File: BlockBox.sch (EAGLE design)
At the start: 95 parts, among them Q100 TK3R1E04PL, Q101 TK3R1E04PL, Q102 IPP052N06L3 G, Q103 IPP052N06L3 G, Q104 IPP052N06L3 G, Q105 IPP052N06L3 G, Q106 TK3R1E04PL, Q300 NMOS, U100 BQ77915, U101 MAX1737, U102 LM74700-Q1, U103 LM74700-Q1, U104 LM74700-Q1, U200 LM5022, U300 TPA3255, U301 NCS20071

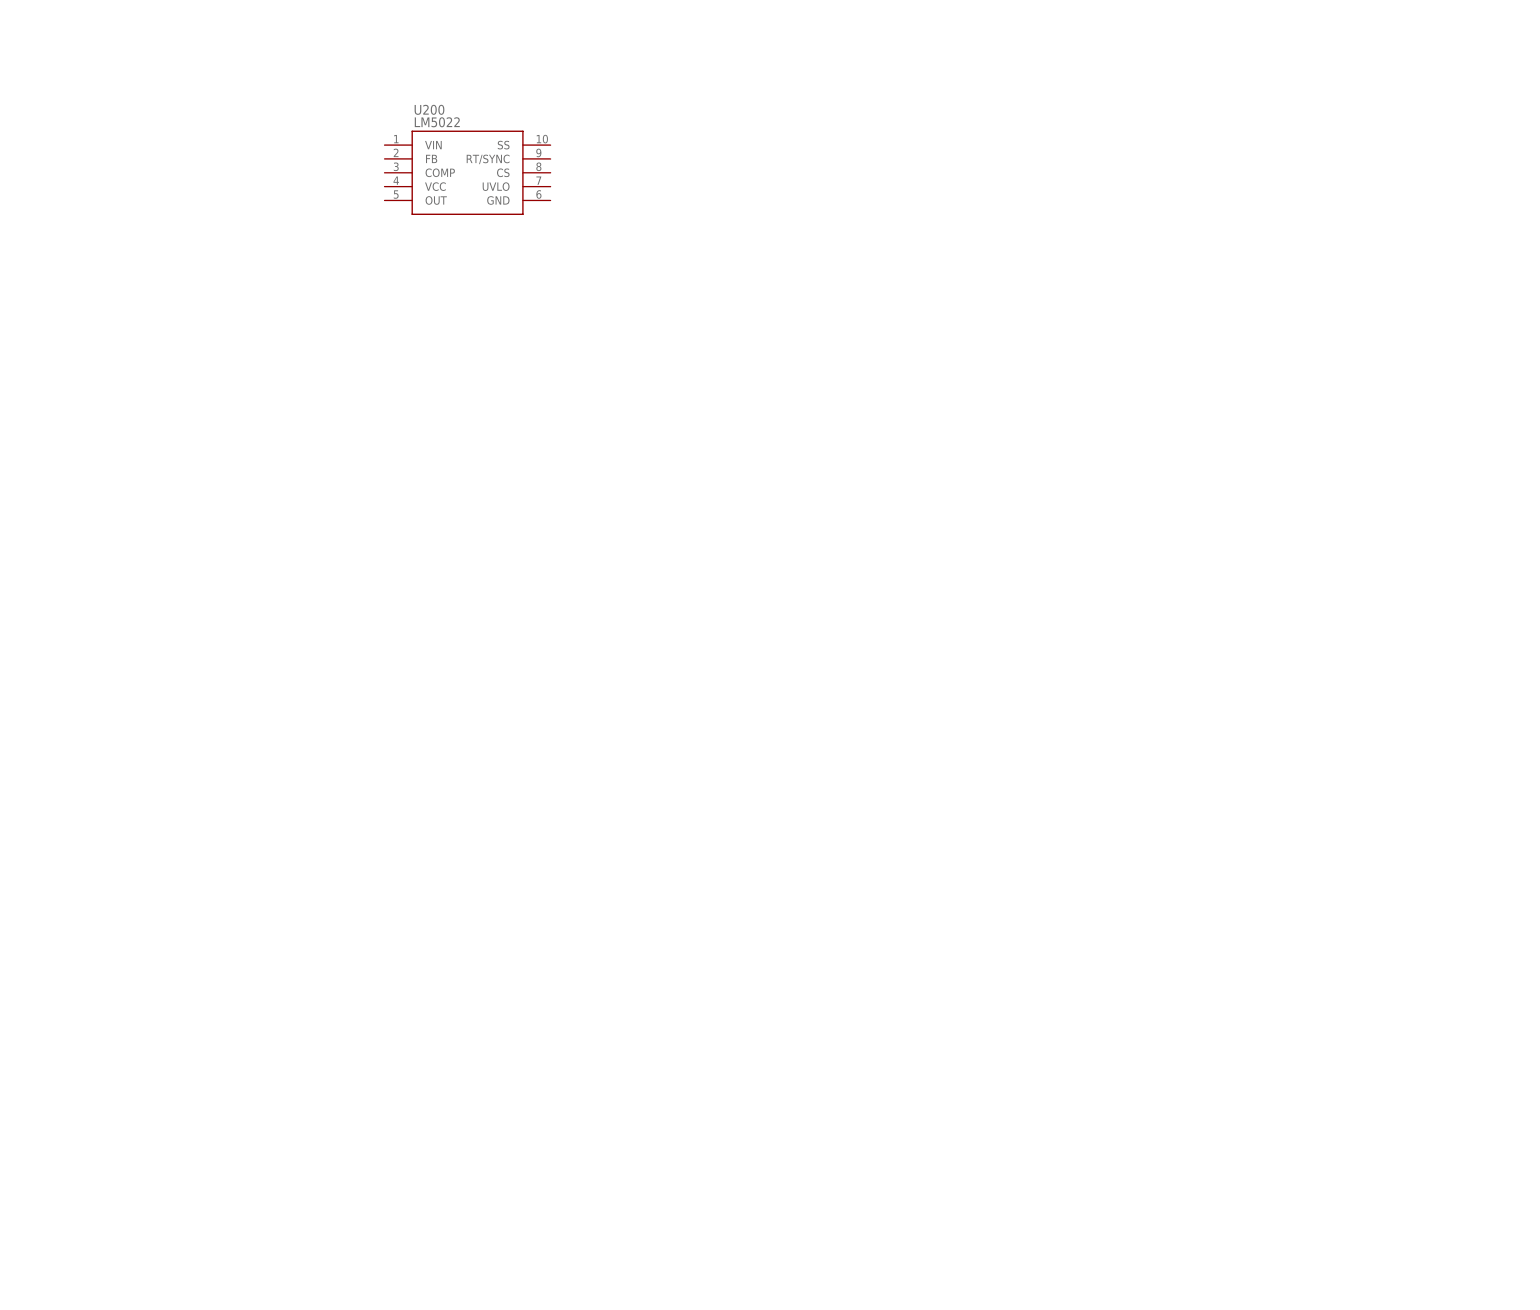
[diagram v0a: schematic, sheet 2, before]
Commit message: Battery management & power converters done (for now).
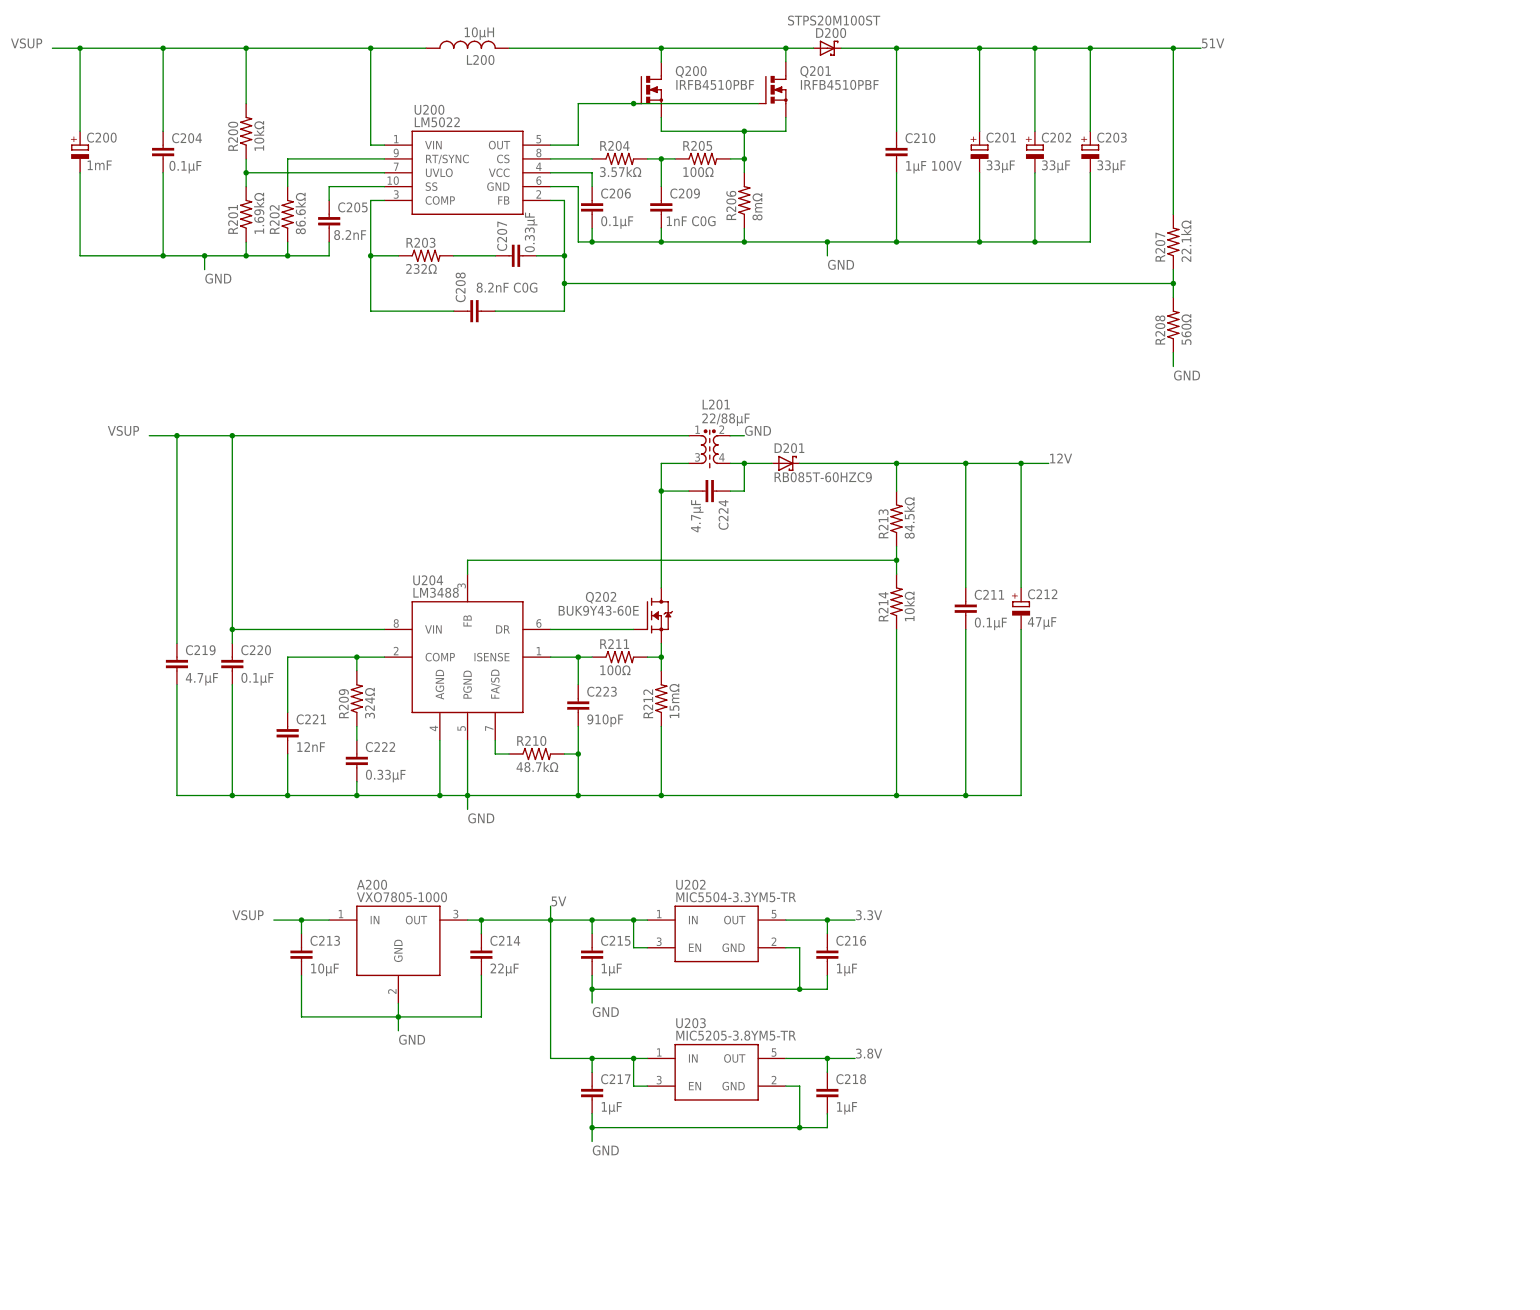
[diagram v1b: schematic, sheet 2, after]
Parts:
- added A200: VXO7805-1000, BW-Active:VXO78
- added C200: 1mF, rcl:CPOL-EUE7.5-16
- added C201, C202, C203: 33µF, rcl:CPOL-EUE3.5-8
- added C204, C206, C211, C220: 0.1µF, rcl:C-EUC0805
- added C205: 8.2nF, rcl:C-EUC0603
- added C207, C222: 0.33µF, rcl:C-EU050-035X075
- added C208: 8.2nF C0G, rcl:C-EUC0603
- added C209: 1nF C0G, rcl:C-EUC0603
- added C210: 1µF 100V, rcl:C-EUC1206
- added C212: 47µF, rcl:CPOL-EUE2.5-6
- added C213: 10µF, rcl:C-EUC1206
- added C214: 22µF, rcl:C-EUC0805
- added C215, C216, C217, C218: 1µF, rcl:C-EUC0603
- added C219, C224: 4.7µF, rcl:C-EUC0805
- added C221: 12nF, rcl:C-EUC0805
- added C223: 910pF, rcl:C-EUC0603
- added D102: 3.9V, BW-Active:SOD323-ZENER
- added D200: STPS20M100ST, BW-Active:TO220AB-SCHOTTKY
- added D201: RB085T-60HZC9, BW-Active:TO220AB-SCHOTTKY
- added L200: 10µH, BW-PassiveMechanical:PQ2614B
- added L201: 22/88µF, BW-PassiveMechanical:SRF1280A
- added Q200, Q201: IRFB4510PBF, transistor-power:PMOSFET_NTO220BV
- added Q202: BUK9Y43-60E, BW-Active:SOT669-N-MOSFET
- added R128, R200, R214: 10kΩ, resistor:R-US_R0805
- added R201: 1.69kΩ, resistor:R-US_R0603
- added R202: 86.6kΩ, resistor:R-US_R0603
- added R203: 232Ω, resistor:R-US_R0603
- added R204: 3.57kΩ, resistor:R-US_R0603
- added R205, R211: 100Ω, resistor:R-US_R0603
- added R206: 8mΩ, resistor:R-US_R1206
- added R207: 22.1kΩ, resistor:R-US_R0603
- added R208: 560Ω, resistor:R-US_R0603
- added R209: 324Ω, resistor:R-US_R0603
- added R210: 48.7kΩ, resistor:R-US_R0603
- added R212: 15mΩ, BW-PassiveMechanical:R-US_R0612
- added R213: 84.5kΩ, resistor:R-US_R0603
- added U202: MIC5504-3.3YM5-TR, BW-Active:SOT23-5-LDO
- added U203: MIC5205-3.8YM5-TR, BW-Active:SOT23-5-LDO
- added U204: LM3488, BW-Active:LM3488
- C105, C106, C107, C110: device resistor:C-EUC0805 -> rcl:C-EUC0805
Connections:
- removed net VIN_EXT1: C128.1
- removed net VIN_EXT3: C135.1
- removed net VIN_EXT5: C132.1
- new net 3.3V: C216.1, U202.OUT
- new net 3.8V: C218.1, U203.OUT
- new net 51V: C201.+, C202.+, C203.+, C210.1, D200.C, R207.2
- new net 5V: A200.OUT, C214.1, C215.1, C217.1, U202.EN, U202.IN, U203.EN, U203.IN
- new net BOOST_COMP: C208.1, R203.1, U200.COMP
- new net BOOST_COMP_INT: C207.1, R203.2
- new net BOOST_CS: R204.1, U200.CS
- new net BOOST_CS_FILTER: C209.1, R204.2, R205.1
- new net BOOST_FB: C207.2, C208.2, R207.1, R208.2, U200.FB
- new net BOOST_RT: R202.2, U200.RT/SYNC
- new net BOOST_SS: C205.1, U200.SS
- new net BOOST_SW_DRAIN: D200.A, L200.2, Q200.D, Q201.D
- new net BOOST_SW_GATE: Q200.G, Q201.G, U200.OUT
- new net BOOST_SW_SOURCE: Q200.S, Q201.S, R205.2, R206.2
- new net BOOST_UVLO: R200.1, R201.2, U200.UVLO
- new net BOOST_VCC: C206.1, U200.VCC
- new net SEPIC_COMP: C221.1, R209.2, U204.COMP
- new net SEPIC_COMP_INT: C222.1, R209.1
- new net SEPIC_FA: R210.1, U204.FA/SD
- new net SEPIC_FB: R213.1, R214.2, U204.FB
- new net SEPIC_ISENSE: C223.1, R211.1, U204.ISENSE
- new net SEPIC_PREDIODE: C224.1, D201.A, L201.S2
- new net SEPIC_SW_DRAIN: C224.2, L201.P2, Q202.D
- new net SEPIC_SW_GATE: Q202.G, U204.DR
- new net SEPIC_SW_SOURCE: Q202.S, R211.2, R212.2
- net !CHG_SHDN: now also D102.C, R128.2
- net 12V: now also C211.1, C212.+, D201.C, R213.2
- net BAT_CHG_CTL: now also R128.1
- net CHG_CSSP: now also C128.1
- net GND: now also A200.GND, C200.-, C201.-, C202.-, C203.-, C204.2, C205.2, C206.2, C209.2, C210.2, C211.2, C212.-, C213.2, C214.2, C215.2, C216.2, C217.2, C218.2, C219.2, C220.2, C221.2, C222.2, C223.2, D102.A, L201.S1, R201.1, R202.1, R206.1, R208.1, R210.2, R212.1, R214.1, U200.GND, U202.GND, U203.GND, U204.AGND, U204.PGND
- net VSUP: now also A200.IN, C132.1, C135.1, C200.+, C204.1, C213.1, C219.1, C220.1, L200.1, L201.P1, R200.2, U200.VIN, U204.VIN
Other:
- moved on the sheet: U200

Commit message: Changed 12V converter, added audio crossover & preamp stage
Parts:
- added A400: BM62, BW-Active:BM62
- added C300, C301, C302, C307, C308, C309, C315, C321: 10µF, rcl:C-EUC0805
- added C303, C305, C310, C312, C316, C318: 330pF, rcl:C-EUC0603
- added C304, C306, C311, C313, C317, C319: 1nF C0G, rcl:C-EUC0603
- added C314, C320: 10µF?, rcl:C-EUC0805
- added F300: 2A, BW-PassiveMechanical:MRF_FUSE
- added F301, F302: 1A, BW-PassiveMechanical:MRF_FUSE
- added R304, R305, R306, R307, R308, R309, R314, R315, R316, R317, R322, R323, R328, R329: 10kΩ, resistor:R-US_R0805
- added R310, R312: 133kΩ, resistor:R-US_R0603
- added R311, R313: 35.7kΩ, resistor:R-US_R0603
- added R318, R320, R324, R326: 113kΩ, resistor:R-US_R0603
- added R319, R321, R325, R327: 42.2kΩ, resistor:R-US_R0603
- added RV300: 20kΩ, BW-PassiveMechanical:TC33X-2
- added RV301, RV302: 10kΩ, BW-PassiveMechanical:TC33X-2
- added U302, U303, U304: LM2902, BW-Active:LM2902
- Q100, Q101, Q102, Q103, Q104, Q105, Q106, Q200, Q201: device transistor-power:PMOSFET_NTO220BV -> BW-Active:TO220BV-N-MOSFET
- R203: value 232Ω -> 237Ω
- R207: value 22.1kΩ -> 23.2kΩ
- R208: value 560Ω -> 576Ω
- R302: value 36kΩ -> 39kΩ
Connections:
- net 51V renamed 52V
- new net 6V: C300.1, C303.1, C305.1, R304.1, R305.2, R318.1, R320.1, R324.1, R326.1, U302A.+IN, U302B.+IN, U303C.+IN, U303D.+IN, U304B.+IN, U304C.+IN
- new net AMP_IN_A: C308.2, U300.INPUT_A
- new net AMP_IN_B: C309.2, U300.INPUT_B
- new net AMP_IN_C: C315.2, U300.INPUT_C
- new net AMP_IN_D: C321.2, U300.INPUT_D
- new net AUD_SRC_L: A400.SPKL, C301.1
- new net AUD_SRC_R: A400.SPKR, C302.1
- new net PA_LH1_FB: C310.2, C311.1, R319.1
- new net PA_LH1_FILT: C311.2, R318.2, U302D.+IN
- new net PA_LH1_OUT: C312.1, R319.2, U302D.-IN, U302D.OUT
- new net PA_LH2_FB: C312.2, C313.1, R321.1
- new net PA_LH2_FILT: C313.2, R320.2, U303A.+IN
- new net PA_LH2_OUT: C314.1, R321.2, U303A.-IN, U303A.OUT
- new net PA_LH_COUPLE: C314.2, R322.1
- new net PA_LH_FINAL: C315.1, RV301.S, U303D.OUT
- new net PA_LH_GFB: R322.2, R323.1, U303D.-IN
- new net PA_LH_GFB_VAR: R323.2, RV301.A
- new net PA_LL1_FB: C304.1, R310.2, R311.1
- new net PA_LL1_FILT: C303.2, R311.2, U304A.+IN
- new net PA_LL1_OUT: C304.2, R312.1, U304A.-IN, U304A.OUT
- new net PA_LL2_FB: C306.1, R312.2, R313.1
- new net PA_LL2_FILT: C305.2, R313.2, U304D.+IN
- new net PA_LL2_OUT: C306.2, C307.1, U304D.-IN, U304D.OUT
- new net PA_LL_COUPLE: C307.2, R314.1
- new net PA_LL_FINAL+: C308.1, R316.1, RV300.S, U304C.OUT
- new net PA_LL_FINAL-: C309.1, R317.2, U304B.OUT
- new net PA_LL_GFB: R314.2, R315.1, U304C.-IN
- new net PA_LL_GFB_VAR: R315.2, RV300.A
- new net PA_LL_IFB: R316.2, R317.1, U304B.-IN
- new net PA_L_IN_BUFFERED: C310.1, R307.2, R310.1, U302A.OUT
- new net PA_L_IN_COUPLE: C301.2, R306.1
- new net PA_L_IN_FB: R306.2, R307.1, U302A.-IN
- new net PA_RH1_FB: C316.2, C317.1, R325.1
- new net PA_RH1_FILT: C317.2, R324.2, U302C.+IN
- new net PA_RH1_OUT: C318.1, R325.2, U302C.-IN, U302C.OUT
- new net PA_RH2_FB: C318.2, C319.1, R327.1
- new net PA_RH2_FILT: C319.2, R326.2, U303B.+IN
- new net PA_RH2_OUT: C320.1, R327.2, U303B.-IN, U303B.OUT
- new net PA_RH_COUPLE: C320.2, R328.1
- new net PA_RH_FINAL: C321.1, RV302.S, U303C.OUT
- new net PA_RH_GFB: R328.2, R329.1, U303C.-IN
- new net PA_RH_GFB_VAR: R329.2, RV302.A
- new net PA_R_IN_BUFFERED: C316.1, R309.2, U302B.OUT
- new net PA_R_IN_COUPLE: C302.2, R308.1
- new net PA_R_IN_FB: R308.2, R309.1, U302B.-IN
- net 12V: now also R304.2, U302A.V+, U303A.V+, U304A.V+
- net GND: now also C300.2, R305.1, U302A.V-, U303A.V-, U304A.V-

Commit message: Audio path finished, revised 5V supply
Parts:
- removed A200: VXO7805-1000, BW-Active:VXO78
- added C225, C226: 1nF, rcl:C-EUC0603
- added C227: 47µF, rcl:CPOL-EUE2.5-6
- added C322: 470µF, rcl:CPOL-EUE3.5-8
- added C323, C324, C329: 0.1µF, rcl:C-EUC0805
- added C325, C326, C327, C328: 1µF, rcl:C-EUC0603
- added C330, C331, C332, C333: 33nF, rcl:C-EUC0805
- added C334, C335, C337, C338, C340, C343, C346, C349: 1µF 100V, rcl:C-EUC1206
- added C336, C339, C352, C353: 470µF 80V, rcl:CPOL-EUE5-13
- added C341, C344, C347, C350: 1nF 100V, rcl:C-EUC1206
- added C342, C345, C348, C351: 10nF, rcl:C-EUC1206
- added D202: SK44BL-TP, BW-Active:DO-214AA-SCHOTTKY
- added J100: PWRSW, BW-Connectors:GEN-2PIN
- added L202: 10µH, BW-PassiveMechanical:SRN1060
- added L300, L301: 10µH, BW-PassiveMechanical:RCH8011
- added L302, L303: 15µH, BW-PassiveMechanical:RCH8011
- added Q203: DMP4065S-7, BW-Active:SOT23-P-MOSFET
- added R215: 44.2kΩ, resistor:R-US_R0603
- added R216: 1.43kΩ, resistor:R-US_R0603
- added R217: 10mΩ, resistor:R-US_R1206
- added R218: 10kΩ, resistor:R-US_R0805
- added R219: 3.32kΩ, resistor:R-US_R0603
- added R330, R331, R334, R335, R336, R337: 3.3Ω, resistor:R-US_R0805
- added R332: 64.9kΩ, resistor:R-US_R0603
- added R333: 30kΩ, resistor:R-US_R0603
- added U201: LM3488, BW-Active:LM3488
- C209, C304, C306, C311, C313, C317, C319: value 1nF C0G -> 1nF
- C214: value 22µF -> 0.47µF; device rcl:C-EUC0805 -> rcl:C-EUC0603
- C305: value 330pF -> 100pF
- FAN300: value HA30101V3-000U-A99 -> HA30101V3
- R310: value 133kΩ -> 200kΩ
- R311: value 35.7kΩ -> 24.3kΩ
- R312: value 133kΩ -> 237kΩ
- R313: value 35.7kΩ -> 66.5kΩ
- R318, R324: value 113kΩ -> 86.6kΩ
- R319, R325: value 42.2kΩ -> 54.9kΩ
- R320, R326: value 113kΩ -> 210kΩ
- R321, R327: value 42.2kΩ -> 22.6kΩ
- U202: value MIC5504-3.3YM5-TR -> LM25085; device BW-Active:SOT23-5-LDO -> BW-Active:LM25085
- U203: value MIC5205-3.8YM5-TR -> MIC5504-3.3YM5-TR
- U204: value LM3488 -> MIC5205-3.8YM5-TR; device BW-Active:LM3488 -> BW-Active:SOT23-5-LDO
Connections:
- new net AMP_!CLIP_OTW: U300.!CLIP_OTW
- new net AMP_!FAULT: U300.!FAULT
- new net AMP_!RESET: U300.!RESET
- new net AMP_AVDD: C326.1, U300.AVDD
- new net AMP_A_FILT: C340.1, C341.1, C342.1, F300.1, L300.2
- new net AMP_A_FILT_INT: C342.2, R334.2
- new net AMP_A_FUSED: F300.2, XLS300.1
- new net AMP_BST_A: C330.1, U300.BST_A
- new net AMP_BST_B: C331.1, U300.BST_B
- new net AMP_BST_C: C332.2, U300.BST_C
- new net AMP_BST_D: C333.2, U300.BST_D
- new net AMP_B_FILT: C343.2, C344.2, C345.2, L301.2, XLS300.2
- new net AMP_B_FILT_INT: C345.1, R335.2
- new net AMP_CSTART: C327.1, U300.C_START
- new net AMP_C_COUPLED: C352.-, F301.1
- new net AMP_C_FILT: C346.1, C347.1, C348.1, C352.+, L302.2
- new net AMP_C_FILT_INT: C348.2, R336.2
- new net AMP_C_FUSED: F301.2, XLS301.1
- new net AMP_DVDD: C325.1, U300.DVDD, U300.M1
- new net AMP_D_COUPLED: C353.-, F302.1
- new net AMP_D_FILT: C349.2, C350.2, C351.2, C353.+, L303.2
- new net AMP_D_FILT_INT: C351.1, R337.2
- new net AMP_D_FUSED: F302.2, XLS302.1
- new net AMP_FREQ_ADJ: R333.2, U300.FREQ_ADJ
- new net AMP_GVDD_AB: C324.1, R330.2, U300.GVDD_AB
- new net AMP_GVDD_CD: C329.1, R331.2, U300.GVDD_CD
- new net AMP_OC_ADJ: R332.2, U300.OC_ADJ
- new net AMP_OUT_A: C330.2, L300.1, U300.OUT_A
- new net AMP_OUT_B: C331.2, L301.1, U300.OUT_B
- new net AMP_OUT_C: C332.1, L302.1, U300.OUT_C
- new net AMP_OUT_D: L303.1, U300.OUT_D
- new net AMP_VBG: C328.1, U300.VBG
- new net BAT_PRES_SW: J100B.P$1, R116.2
- new net BUCK_ADJ: C225.2, R216.1, U202.ADJ
- new net BUCK_FB: R218.1, R219.2, U202.FB
- new net BUCK_RT: R215.1, U202.RT
- new net BUCK_SW_DRAIN: Q203.S, R217.1, U202.ISEN
- new net BUCK_SW_GATE: Q203.G, U202.PGATE
- new net BUCK_SW_SOURCE: D202.C, L202.1, Q203.D
- new net BUCK_VCC: C214.2, U202.VCC
- net 12V: now also C322.+, C323.1, R330.1, R331.1, U300.VDD
- net 3.3V: now also U203.OUT; no longer U202.OUT
- net 3.8V: now also U204.OUT; no longer U203.OUT
- net 52V: now also C333.1, C334.1, C335.1, C336.+, C337.1, C338.1, C339.+, U300.PVDD_AB, U300.PVDD_CD
- net 5V: now also C226.1, C227.+, L202.2, R218.2, U204.EN, U204.IN; no longer A200.OUT, C214.1, U202.EN, U202.IN
- net BAT_VDD: now also J100A.P$1; no longer R116.2
- net GND: now also C226.2, C227.-, C322.-, C323.2, C324.2, C325.2, C326.2, C327.2, C328.2, C329.2, C334.2, C335.2, C336.-, C337.2, C338.2, C339.-, C340.2, C341.2, C343.1, C344.1, C346.2, C347.2, C349.1, C350.1, D202.A, R219.1, R332.1, R333.1, R334.1, R335.1, R336.1, R337.1, U201.AGND, U201.PGND, U204.GND, U300.M2, XLS301.2, XLS302.2; no longer A200.GND, C214.2, U204.AGND, U204.PGND
- net SEPIC_COMP: now also U201.COMP; no longer U204.COMP
- net SEPIC_FA: now also U201.FA/SD; no longer U204.FA/SD
- net SEPIC_FB: now also U201.FB; no longer U204.FB
- net SEPIC_ISENSE: now also U201.ISENSE; no longer U204.ISENSE
- net SEPIC_SW_GATE: now also U201.DR; no longer U204.DR
- net VSUP: now also C214.1, C225.1, R215.2, R216.2, R217.2, U201.VIN, U202.VIN; no longer A200.IN, U204.VIN
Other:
- moved on the sheet: C213, C214, C215, C216, C217, C218, F300, F301, F302, FAN300, H300, Q300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

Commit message: Changed bass input to summing amp (L+R), added preliminary BM62 configs.
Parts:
- added C354, C355: 10µF, rcl:C-EUC0805
- added R338, R339, R340: 10kΩ, resistor:R-US_R0805
- added U305: NCS20071, BW-Active:NCS20071
- C213: value 10µF -> 10µF 35V
- R315: value 10kΩ -> 4.53kΩ; device resistor:R-US_R0805 -> resistor:R-US_R0603
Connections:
- net PA_LH1_FB renamed PA_L1_FB
- net PA_LH1_FILT renamed PA_L1_FILT
- net PA_LH1_OUT renamed PA_L1_OUT
- net PA_LH2_FB renamed PA_L2_FB
- net PA_LH2_FILT renamed PA_L2_FILT
- net PA_LH2_OUT renamed PA_L2_OUT
- net PA_LH_COUPLE renamed PA_L_COUPLE
- net PA_LH_FINAL renamed PA_L_FINAL
- net PA_LH_GFB renamed PA_L_GFB
- net PA_LH_GFB_VAR renamed PA_L_GFB_VAR
- net PA_LL1_FB renamed PA_B1_FB
- net PA_LL1_FILT renamed PA_B1_FILT
- net PA_LL1_OUT renamed PA_B1_OUT
- net PA_LL2_FB renamed PA_B2_FB
- net PA_LL2_FILT renamed PA_B2_FILT
- net PA_LL2_OUT renamed PA_B2_OUT
- net PA_LL_COUPLE renamed PA_B_COUPLE
- net PA_LL_FINAL+ renamed PA_B_FINAL+
- net PA_LL_FINAL- renamed PA_B_FINAL-
- net PA_LL_GFB renamed PA_B_GFB
- net PA_LL_GFB_VAR renamed PA_B_GFB_VAR
- net PA_LL_IFB renamed PA_B_IFB
- net PA_RH1_FB renamed PA_R1_FB
- net PA_RH1_FILT renamed PA_R1_FILT
- net PA_RH1_OUT renamed PA_R1_OUT
- net PA_RH2_FB renamed PA_R2_FB
- net PA_RH2_FILT renamed PA_R2_FILT
- net PA_RH2_OUT renamed PA_R2_OUT
- net PA_RH_COUPLE renamed PA_R_COUPLE
- net PA_RH_FINAL renamed PA_R_FINAL
- net PA_RH_GFB renamed PA_R_GFB
- net PA_RH_GFB_VAR renamed PA_R_GFB_VAR
- new net PA_BL_COUPLE: C354.1, R338.1
- new net PA_BR_COUPLE: C355.1, R339.1
- new net PA_B_IN_BUFFERED: R310.1, R340.2, U305.OUT
- new net PA_B_IN_SUM: R338.2, R339.2, R340.1, U305.-IN
- net 12V: now also U305.V+
- net 6V: now also U305.+IN
- net GND: now also U305.V-
- net PA_L_IN_BUFFERED: now also C354.2; no longer R310.1
- net PA_R_IN_BUFFERED: now also C355.2
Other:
- moved on the sheet: C301, C302, R306, R307, R308, R309, U302A, U302B
